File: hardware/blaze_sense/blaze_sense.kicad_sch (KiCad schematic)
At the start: 65 parts, among them J1 JTAG, SW1 SW_SPST, SW2 SW_SPDT, U1 ADXL375, U2 BMI088, U3 A3G4250D, U4 ADXL345, U5 MS5611-01BA, U6 RM3100, U7 STM32H573AIIx, U8 TCAN1044VDDFR, Y1 ABM3-8.000MHZ-B4Y-T, Y2 ABS07-32.768KHZ-T

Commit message: Removed audio, neopixel, can2 from interconnect
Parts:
- added J2: Conn_01x30, symbol Connector_Generic:Conn_01x30
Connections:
- net +3V3: now also J2.12 (Pin_12), J2.18 (Pin_18), J2.29 (Pin_29), J2.30 (Pin_30)
- net +5V: now also J2.11 (Pin_11), J2.27 (Pin_27), J2.28 (Pin_28)
- net CANH: now also J2.24 (Pin_24)
- net CANL: now also J2.23 (Pin_23)
- net GND: now also J2.14 (Pin_14), J2.15 (Pin_15), J2.21 (Pin_21), J2.22 (Pin_22), J2.3 (Pin_3), J2.4 (Pin_4)
- net PPS: now reaches U7.K6 (PB1)
- net PPS: now also J2.13 (Pin_13)
- net ARM: now reaches U7.L5 (PB0)
- net ARM: now also J2.8 (Pin_8)
- new net RX_RADIO: J2.6 (Pin_6)
- new net TX_RADIO: J2.5 (Pin_5)
- no-connect marks 109 -> 118

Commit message: Sense Footprint Assignments
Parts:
- C1, C10, C11, C12, C13, C14, C15, C16, C17, C18, C19, C2, C20, C21, C22, C23, C24, C25, C26, C27, C28, C29, C3, C30, C31, C32, C33, C34, C4, C5, C6, C7, C8, C9: footprint (none) -> Capacitor_SMD:C_0603_1608Metric
- D1: footprint (none) -> Diode_SMD:D_0603_1608Metric
- J2: footprint (none) -> DF17:HRS_DF17_1.0H_-30DP-0.5V_57_
- R1, R10, R11, R12, R2, R3, R4, R5, R6, R7, R8, R9: footprint (none) -> Resistor_SMD:R_0603_1608Metric
- SW1: footprint (none) -> Button_Switch_SMD:SW_SPST_B3U-1000P
- SW2: footprint (none) -> Button_Switch_SMD:Nidec_Copal_CAS-120A
- U8: footprint (none) -> Package_SON:Texas_VSON-HR-8_1.5x2mm_P0.5mm

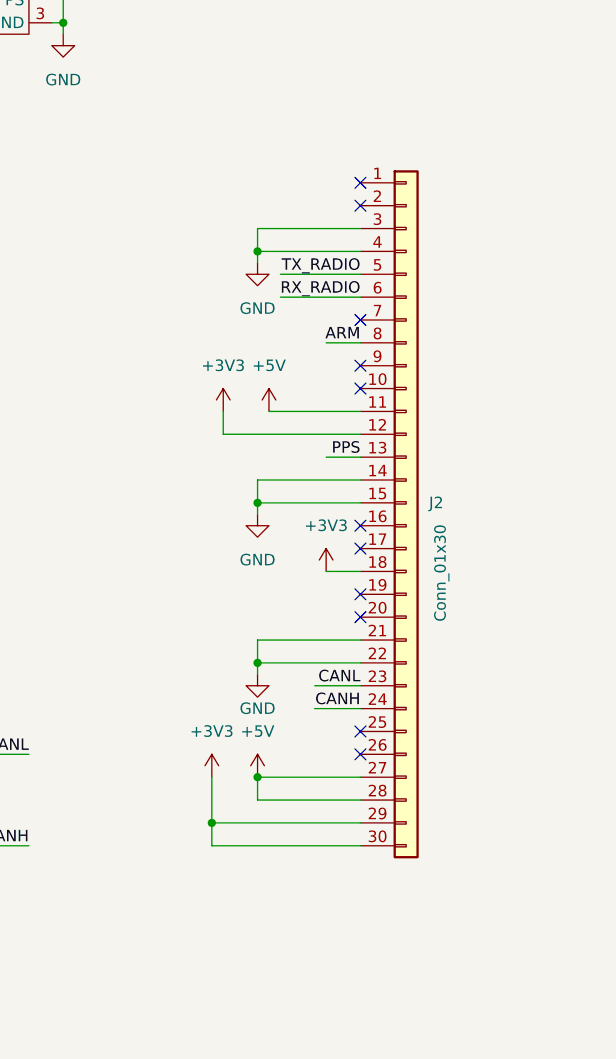
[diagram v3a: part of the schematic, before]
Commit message: Added mirror interconnect and PCB to sense
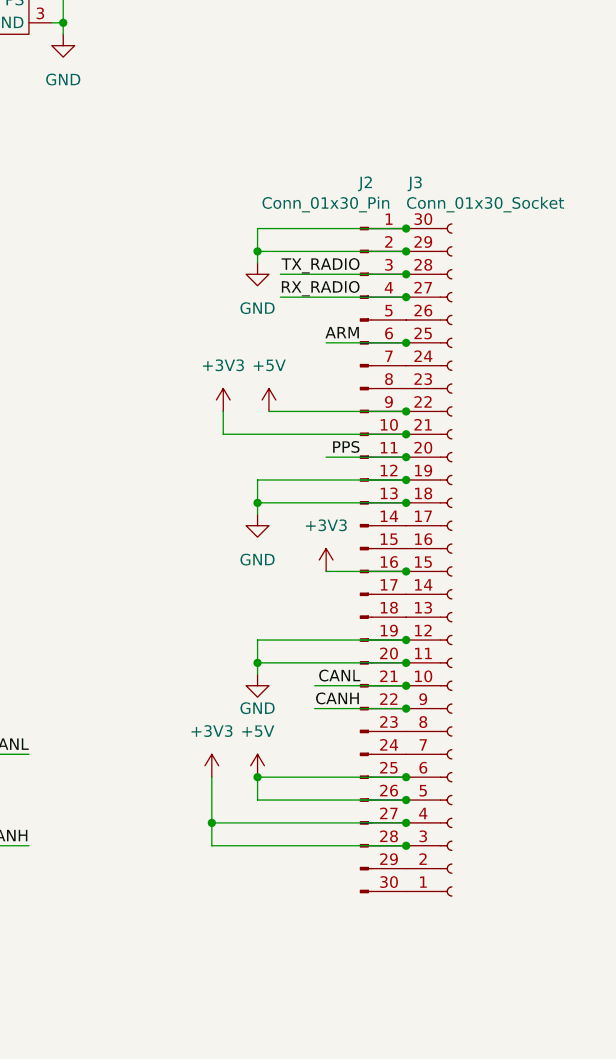
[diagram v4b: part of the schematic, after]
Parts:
- removed J2: Conn_01x30, DF17:HRS_DF17_1.0H_-30DP-0.5V_57_, symbol Connector_Generic:Conn_01x30
- added J2: Conn_01x30_Pin, Blaze_Library:HRS_DF17_1.0H_-30DP-0.5V_57_, symbol Connector:Conn_01x30_Pin
- added J3: Conn_01x30_Socket, Blaze_Library:HRS_DF17_1.0H_-30DP-0.5V_57_, symbol Connector:Conn_01x30_Socket
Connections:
- net +3V3: now also J2.10 (Pin_10), J2.16 (Pin_16), J2.27 (Pin_27), J2.28 (Pin_28), J3.15 (Pin_15), J3.21 (Pin_21), J3.3 (Pin_3), J3.4 (Pin_4)
- net +5V: now also J2.25 (Pin_25), J2.26 (Pin_26), J2.9 (Pin_9), J3.22 (Pin_22), J3.5 (Pin_5), J3.6 (Pin_6)
- net ARM: now also J2.6 (Pin_6), J3.25 (Pin_25)
- net CANH: now also J2.22 (Pin_22), J3.9 (Pin_9)
- net CANL: now also J2.21 (Pin_21), J3.10 (Pin_10)
- net GND: now also J2.1 (Pin_1), J2.12 (Pin_12), J2.13 (Pin_13), J2.19 (Pin_19), J2.2 (Pin_2), J2.20 (Pin_20), J3.11 (Pin_11), J3.12 (Pin_12), J3.18 (Pin_18), J3.19 (Pin_19), J3.29 (Pin_29), J3.30 (Pin_30)
- net PPS: now also J2.11 (Pin_11), J3.20 (Pin_20)
- net RX_RADIO: now also J2.4 (Pin_4), J3.27 (Pin_27)
- net TX_RADIO: now also J2.3 (Pin_3), J3.28 (Pin_28)
- new net: J2.30 (Pin_30), J3.1 (Pin_1)
- new net: J2.18 (Pin_18), J3.13 (Pin_13)
- new net: J2.17 (Pin_17), J3.14 (Pin_14)
- new net: J2.15 (Pin_15), J3.16 (Pin_16)
- new net: J2.14 (Pin_14), J3.17 (Pin_17)
- new net: J2.29 (Pin_29), J3.2 (Pin_2)
- new net: J2.8 (Pin_8), J3.23 (Pin_23)
- new net: J2.7 (Pin_7), J3.24 (Pin_24)
- new net: J2.5 (Pin_5), J3.26 (Pin_26)
- new net: J2.24 (Pin_24), J3.7 (Pin_7)
- new net: J2.23 (Pin_23), J3.8 (Pin_8)
- no-connect marks 118 -> 107

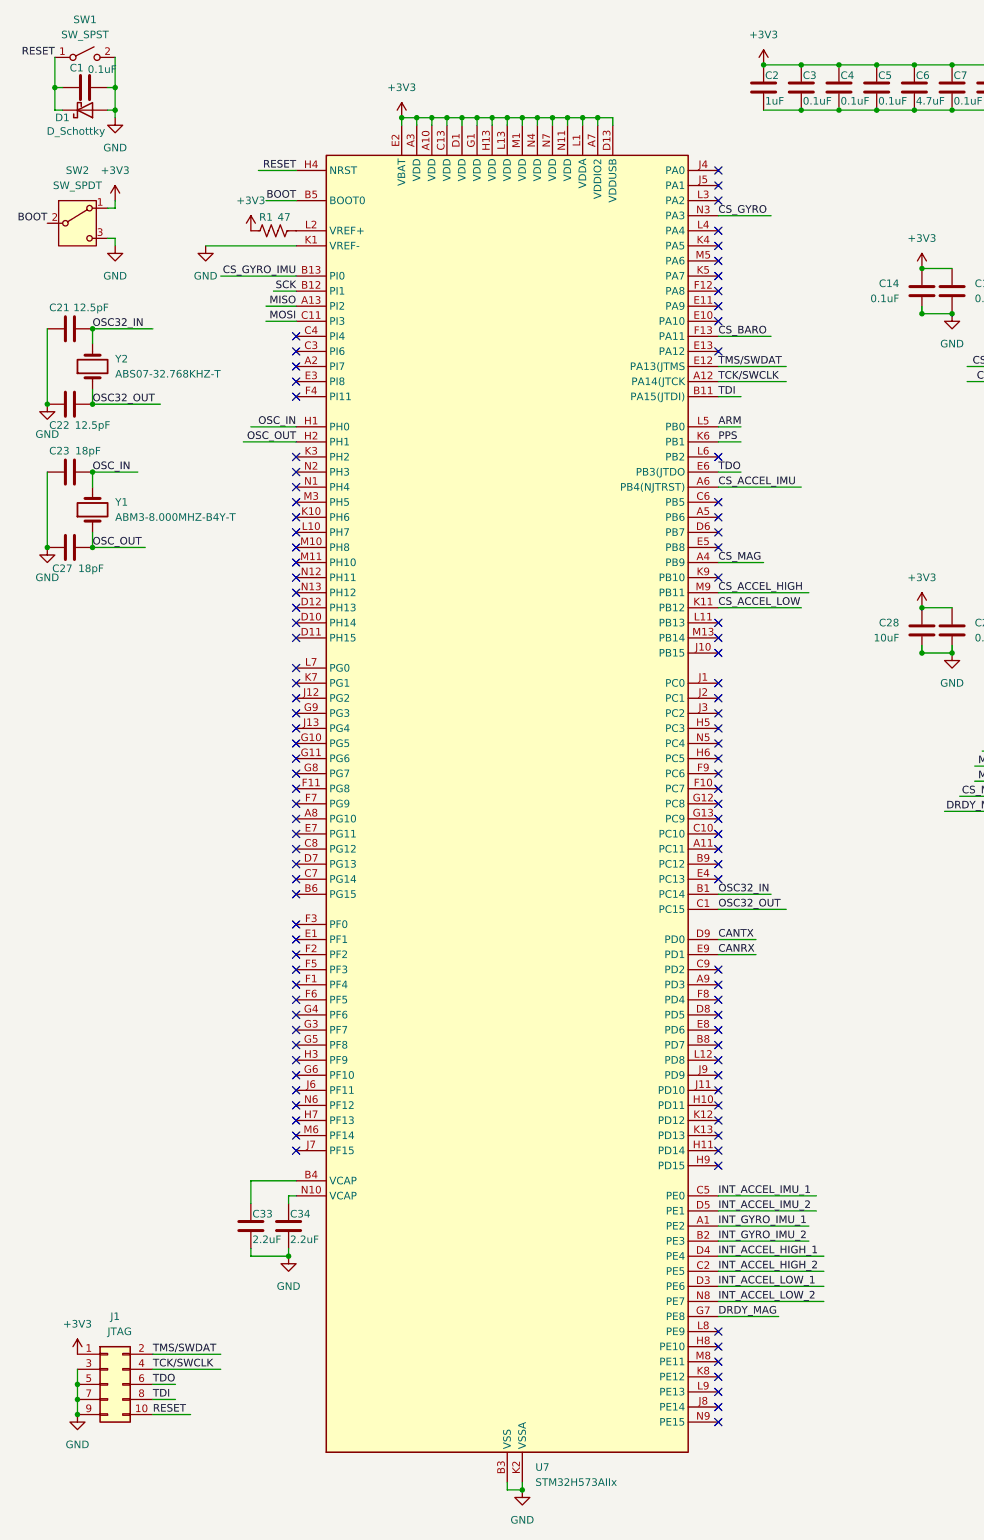
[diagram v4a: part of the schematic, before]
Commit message: Changed MCU
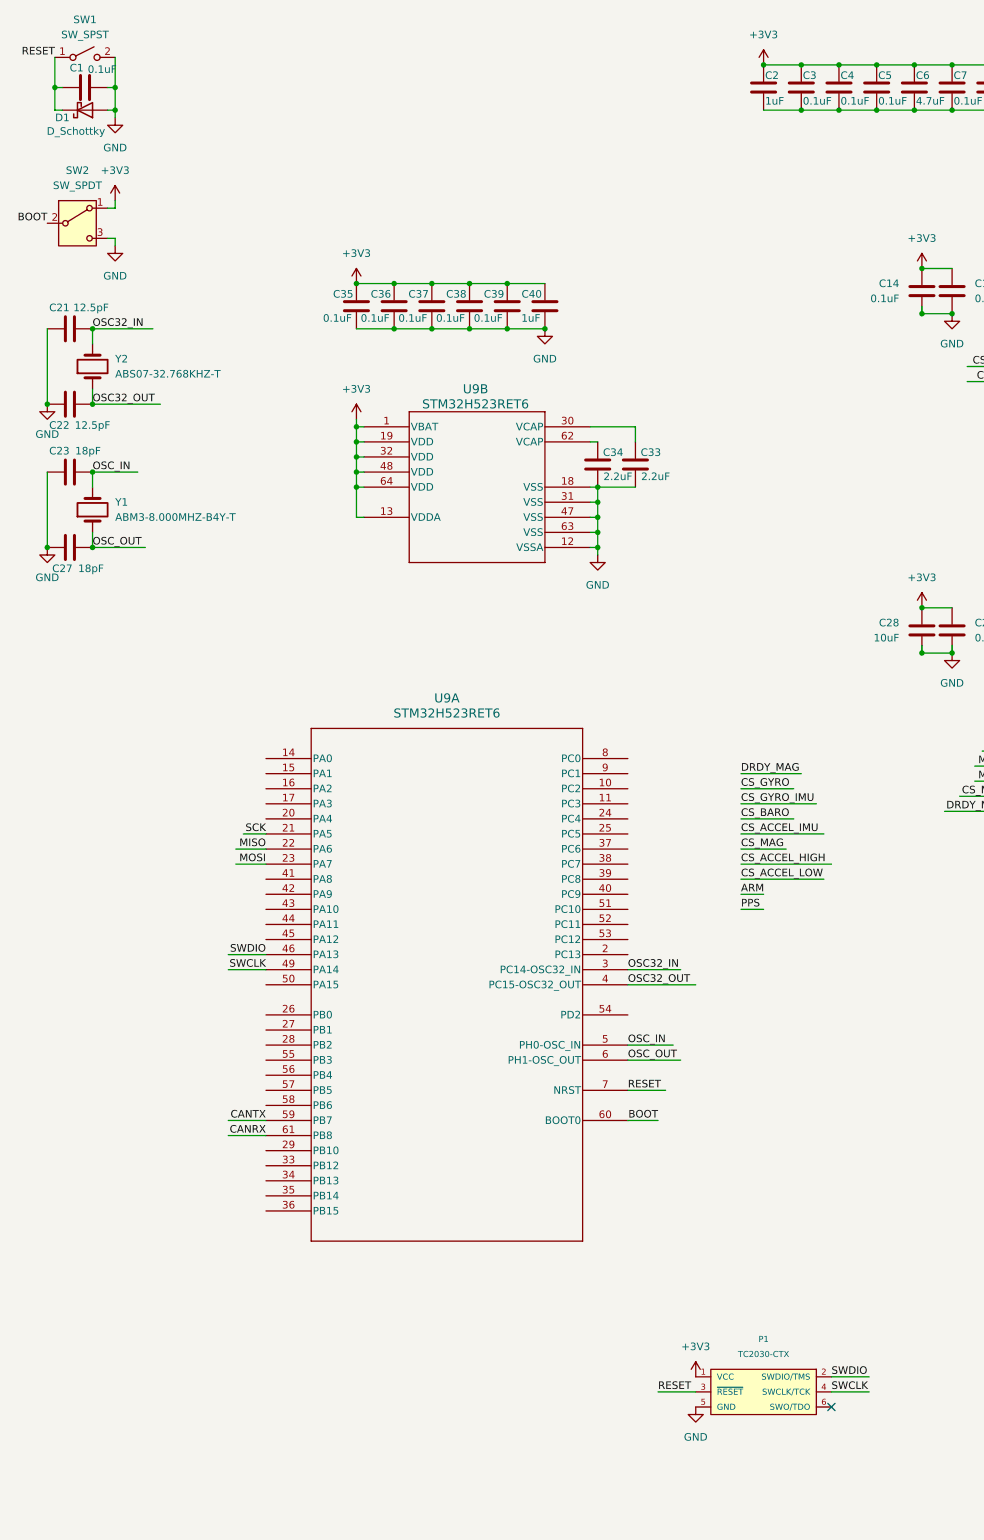
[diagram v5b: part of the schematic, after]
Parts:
- removed J1: JTAG, symbol Connector_Generic:Conn_02x05_Odd_Even
- removed R1: 47, Resistor_SMD:R_0603_1608Metric, symbol Device:R_US
- removed U7: STM32H573AIIx, Package_BGA:UFBGA-169_7x7mm_Layout13x13_P0.5mm, symbol MCU_ST_STM32H5:STM32H573AIIx
- added C35, C36, C37, C38, C39: 0.1uF, Capacitor_SMD:C_0603_1608Metric, symbol Device:C
- added C40: 1uF, Capacitor_SMD:C_0603_1608Metric, symbol Device:C
- added P1: TC2030-CTX, BlazeMini:TC2030-IDC-FP, symbol BlazeMiniLib:TC2030-CTX
- added U9: STM32H523RET6, LQFP64_STM, symbol Blaze_Lib:STM32H523RET6
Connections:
- net +3V3: now also C35.1, C36.1, C37.1, C38.1, C39.1, C40.1, P1.1 (VCC), U9.1 (VBAT), U9.13 (VDDA), U9.19 (VDD), U9.32 (VDD), U9.48 (VDD), U9.64 (VDD)
- net BOOT: now also U9.60 (BOOT0)
- net CANRX: now also U9.61 (PB8)
- net CANTX: now also U9.59 (PB7)
- net GND: now also C35.2, C36.2, C37.2, C38.2, C39.2, C40.2, P1.5 (GND), U9.12 (VSSA), U9.18 (VSS), U9.31 (VSS), U9.47 (VSS), U9.63 (VSS)
- net MISO: now also U9.22 (PA6)
- net MOSI: now also U9.23 (PA7)
- net OSC32_IN: now also U9.3 (PC14-OSC32_IN)
- net OSC32_OUT: now also U9.4 (PC15-OSC32_OUT)
- net OSC_IN: now also U9.5 (PH0-OSC_IN)
- net OSC_OUT: now also U9.6 (PH1-OSC_OUT)
- net RESET: now also P1.3 (~{RESET}), U9.7 (NRST)
- net SCK: now also U9.21 (PA5)
- net at C34.1: now also U9.62 (VCAP)
- net at C33.1: now also U9.30 (VCAP)
- new net SWCLK: P1.4 (SWCLK/TCK), U9.49 (PA14)
- new net SWDIO: P1.2 (SWDIO/TMS), U9.46 (PA13)
- no-connect marks 107 -> 3

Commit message: draft for julian to look over
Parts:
- J2, J3: footprint Blaze_Library:HRS_DF17_1.0H_-30DP-0.5V_57_ -> BlazeLibrary:HRS_DF17_1.0H_-30DP-0.5V_57_
- L1, L2: footprint (none) -> BlazeLibrary:SENSOR-XY-F-RM3100
- L3: footprint (none) -> BlazeLibrary:SENSOR-Z-F-RM3100
- P1: footprint BlazeMini:TC2030-IDC-FP -> BlazeLibrary:TC2030-IDC-FP
- U1: footprint (none) -> BlazeLibrary:ADXL375BCCZ-RL
- U2: footprint (none) -> BlazeLibrary:BMI088
- U3: footprint (none) -> BlazeLibrary:A3G4250D
- U4: footprint (none) -> BlazeLibrary:ADXL345
- U6: footprint (none) -> BlazeLibrary:RM3100-13156
- U9: footprint LQFP64_STM -> BlazeLibrary:LQFP64_STM
- Y2: footprint (none) -> Crystal:Crystal_SMD_3215-2Pin_3.2x1.5mm

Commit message: Updated annotation
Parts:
- renumbered C30 to C1, C7 to C10, C8 to C11, C9 to C12, C10 to C13, C11 to C14, C12 to C15, C13 to C16, C14 to C17, C15 to C18, C16 to C19, C31 to C2, C17 to C20, C18 to C21, C19 to C22, C35 to C23, C36 to C24, C37 to C25, C38 to C26, C39 to C27, C40 to C28, C20 to C29, C32 to C3, C21 to C30, C22 to C31, C34 to C32, C23 to C34, C24 to C35, C25 to C36, C26 to C37, C27 to C38, C28 to C39, C1 to C4, C29 to C40, C2 to C5, C3 to C6, C4 to C7, C5 to C8, C6 to C9, D2 to D1, D1 to D2, J2 to J1, J3 to J2, R10 to R1, R8 to R10, R9 to R11, R11 to R2, R12 to R3, R2 to R4, R3 to R5, R4 to R6, R5 to R7, R6 to R8, R7 to R9, U8 to U1, U1 to U2, U2 to U3, U3 to U4, U9 to U5, U4 to U6, U5 to U7, U6 to U8, Y2 to Y1, Y1 to Y2
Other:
- moved on the sheet: C1, C2, C3, D1, FL1, J1, J2, R1, R2, R3, U1

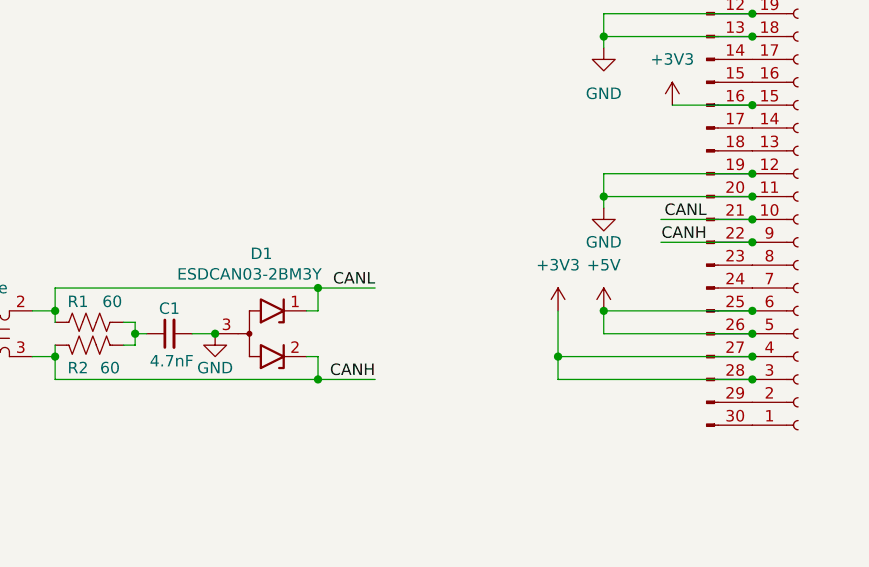
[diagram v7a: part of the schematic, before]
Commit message: Repaired CAN routing
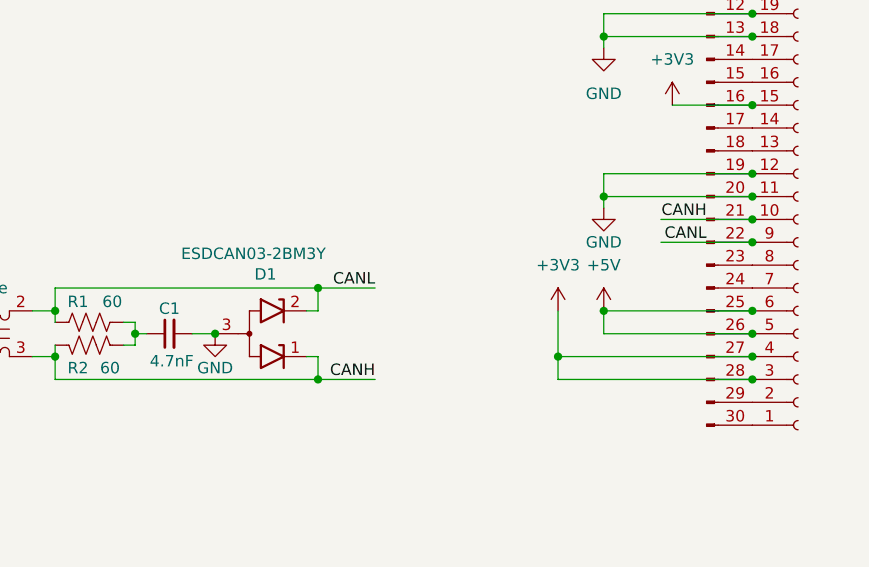
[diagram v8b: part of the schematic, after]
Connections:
- net CANH: now also D1.1 (K1), J1.21 (Pin_21), J2.10 (Pin_10); no longer D1.2 (K2), J1.22 (Pin_22), J2.9 (Pin_9)
- net CANL: now also D1.2 (K2), J1.22 (Pin_22), J2.9 (Pin_9); no longer D1.1 (K1), J1.21 (Pin_21), J2.10 (Pin_10)
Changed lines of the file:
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@@
 	)
 	(junction
+		(at 289.56 210.82)
+		(diameter 0)
+		(color 0 0 0 0)
+	)
+	(junction
 		(at 187.96 114.3)
 		(diameter 0)
@@
 	)
 	(junction
-		(at 289.56 210.82)
-		(diameter 0)
-		(color 0 0 0 0)
-	)
-	(junction
 		(at 349.25 149.86)
 		(diameter 0)
@@
 		)
 	)
-	(label "CANL"
+	(label "CANH"
 		(at 344.17 198.12 180)
 		(fields_autoplaced yes)
@@
 		)
 	)
-	(label "CANH"
+	(label "CANL"
 		(at 344.17 200.66 180)
 		(fields_autoplaced yes)
@@
 		(lib_id "Power_Protection:RCLAMP0582B")
 		(at 294.64 210.82 0)
+		(mirror x)
 		(unit 1)
 		(exclude_from_sim no)
@@
 		(dnp no)
 		(property "Reference" "D1"
-			(at 294.7035 201.93 0)
+			(at 295.148 204.216 0)
 			(effects
 				(font
@@
 		)
 		(property "Value" "ESDCAN03-2BM3Y"
-			(at 293.37 204.216 0)
+			(at 293.8145 201.93 0)
 			(effects
 				(font
@@
 		)
 		(property "Footprint" "Package_TO_SOT_SMD:SOT-416"
-			(at 294.64 218.44 0)
+			(at 294.64 203.2 0)
 			(effects
 				(font
@@
 		)
 		(property "Datasheet" "https://www.semtech.com/products/circuit-protection/low-capacitance/rclamp0582b"
-			(at 295.91 208.28 0)
+			(at 295.91 213.36 0)
 			(effects
 				(font
